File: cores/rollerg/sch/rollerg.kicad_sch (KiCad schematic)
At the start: 1 part

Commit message: wip rollerg sch: objects page
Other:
- added sheet Capacitors (Capacitors.kicad_sch)
- added sheet Not_Populated (Not_Populated.kicad_sch)
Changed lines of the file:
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@@
+	)
+	(sheet
+		(at 246.38 185.42)
+		(size 53.34 20.32)
+		(fields_autoplaced yes)
+		(stroke
+			(width 0.1524)
+			(type solid)
+		)
+		(fill
+			(color 0 0 0 0.0000)
+		)
+		(property "Sheetname" "Capacitors"
+			(at 246.38 184.7084 0)
+			(effects
+				(font
+					(size 3.81 3.81)
+				)
+				(justify left bottom)
+			)
+		)
+		(property "Sheetfile" "Capacitors.kicad_sch"
+			(at 246.38 206.3246 0)
+			(effects
+				(font
+					(size 1.27 1.27)
+				)
+				(justify left top)
+			)
+		)
+		(instances
+			(project "rollerg"
+				(path "/bb61a05c-9ea0-4d47-a326-1f7e835840f3"
+					(page "7")
+				)
+			)
+		)
 	)
 	(sheet
@@
 				)
 			)
+		)
+	)
+	(sheet
+		(at 246.38 215.9)
+		(size 53.34 20.32)
+		(fields_autoplaced yes)
+		(stroke
+			(width 0.1524)
+			(type solid)
+		)
+		(fill
+			(color 0 0 0 0.0000)
+		)
+		(property "Sheetname" "Not_Populated"
+			(at 246.38 215.1884 0)
+			(effects
+				(font
+					(size 3.81 3.81)
+				)
+				(justify left bottom)
+			)
+		)
+		(property "Sheetfile" "Not_Populated.kicad_sch"
+			(at 246.38 236.8046 0)
+			(effects
+				(font
+					(size 1.27 1.27)
+				)
+				(justify left top)
+			)
+		)
+		(instances
+			(project "rollerg"
+				(path "/bb61a05c-9ea0-4d47-a326-1f7e835840f3"
+					(page "8")
+				)
+			)

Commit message: wip rollerg sch: PSAC
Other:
- added sheet IO_Cabinet (IO_Cabinet.kicad_sch)
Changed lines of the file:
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@@
 	)
 	(sheet
-		(at 176.53 33.02)
+		(at 246.38 231.14)
+		(size 53.34 15.24)
+		(fields_autoplaced yes)
+		(stroke
+			(width 0.1524)
+			(type solid)
+		)
+		(fill
+			(color 0 0 0 0.0000)
+		)
+		(property "Sheetname" "IO_Cabinet"
+			(at 246.38 229.1584 0)
+			(effects
+				(font
+					(size 3.81 3.81)
+				)
+				(justify left bottom)
+			)
+		)
+		(property "Sheetfile" "IO_Cabinet.kicad_sch"
+			(at 246.38 246.9646 0)
+			(effects
+				(font
+					(size 1.27 1.27)
+				)
+				(justify left top)
+			)
+		)
+		(instances
+			(project "rollerg"
+				(path "/bb61a05c-9ea0-4d47-a326-1f7e835840f3"
+					(page "9")
+				)
+			)
+		)
+	)
+	(sheet
+		(at 176.53 25.4)
 		(size 52.07 64.77)
 		(fields_autoplaced yes)
@@
 		)
 		(property "Sheetname" "Main"
-			(at 176.53 32.3084 0)
+			(at 176.53 24.6884 0)
 			(effects
 				(font
@@
 		)
 		(property "Sheetfile" "Main.kicad_sch"
-			(at 176.53 98.3746 0)
+			(at 176.53 90.7546 0)
 			(effects
 				(font
@@
 	)
 	(sheet
-		(at 176.53 107.95)
+		(at 176.53 100.33)
 		(size 52.07 68.58)
 		(fields_autoplaced yes)
@@
 		)
 		(property "Sheetname" "Objects"
-			(at 176.53 107.2384 0)
+			(at 176.53 99.6184 0)
 			(effects
 				(font
@@
 		)
 		(property "Sheetfile" "Objects.kicad_sch"
-			(at 176.53 177.1146 0)
+			(at 176.53 169.4946 0)
 			(effects
 				(font
@@
 	)
 	(sheet
-		(at 246.38 107.95)
+		(at 246.38 100.33)
 		(size 53.34 68.58)
 		(fields_autoplaced yes)
@@
 		)
 		(property "Sheetname" "PSAC"
-			(at 246.38 105.9684 0)
+			(at 246.38 98.3484 0)
 			(effects
 				(font
@@
 		)
 		(property "Sheetfile" "PSAC.kicad_sch"
-			(at 246.38 177.1146 0)
+			(at 246.38 169.4946 0)
 			(effects
 				(font
@@
 	)
 	(sheet
-		(at 246.38 33.02)
+		(at 246.38 25.4)
 		(size 53.34 64.77)
 		(fields_autoplaced yes)
@@
 		)
 		(property "Sheetname" "Sound"
-			(at 246.38 31.0384 0)
+			(at 246.38 23.4184 0)
 			(effects
 				(font
@@
 		)
 		(property "Sheetfile" "Sound.kicad_sch"
-			(at 246.38 98.3746 0)
+			(at 246.38 90.7546 0)
 			(effects
 				(font
@@
 	)
 	(sheet
-		(at 246.38 185.42)
-		(size 53.34 20.32)
+		(at 246.38 177.8)
+		(size 53.34 15.24)
 		(fields_autoplaced yes)
 		(stroke
@@
 		)
 		(property "Sheetname" "Capacitors"
-			(at 246.38 184.7084 0)
+			(at 246.38 175.8184 0)
 			(effects
 				(font
@@
 		)
 		(property "Sheetfile" "Capacitors.kicad_sch"
-			(at 246.38 206.3246 0)
+			(at 246.38 193.6246 0)
 			(effects
 				(font
@@
 	)
 	(sheet
-		(at 175.26 185.42)
-		(size 53.34 69.85)
+		(at 176.53 177.8)
+		(size 52.07 69.85)
 		(fields_autoplaced yes)
 		(stroke
@@
 		)
 		(property "Sheetname" "Scroll"
-			(at 175.26 184.7084 0)
+			(at 176.53 175.8184 0)
 			(effects
 				(font
@@
 		)
 		(property "Sheetfile" "Scroll.kicad_sch"
-			(at 175.26 255.8546 0)
+			(at 176.53 248.2346 0)
 			(effects
 				(font
@@
 	)
 	(sheet
-		(at 246.38 215.9)
-		(size 53.34 20.32)
+		(at 246.38 204.47)
+		(size 53.34 15.24)
 		(fields_autoplaced yes)
 		(stroke
@@
 		)
 		(property "Sheetname" "Not_Populated"
-			(at 246.38 215.1884 0)
+			(at 246.38 202.4884 0)
 			(effects
 				(font
@@
 		)
 		(property "Sheetfile" "Not_Populated.kicad_sch"
-			(at 246.38 236.8046 0)
-			(effects
-				(font
+			(at 246.38 220.2946 0)
+			(effects
+				(font

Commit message: wip rollerg sch: SOUND
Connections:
- net COIN_CNT_1: now reaches JM1.8 (COIN_CNT_1)
- net COIN_CNT_2: now reaches JM1.J (COIN_CNT_2)
- no-connect marks 8 -> 6
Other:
- removed sheet Scroll
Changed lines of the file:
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@@
-	)
-	(no_connect
-		(at 54.61 114.3)
 	)
 	(no_connect
@@
 	)
 	(no_connect
-		(at 90.17 114.3)
-	)
-	(no_connect
 		(at 54.61 154.94)
 	)
@@
 	(wire
 		(pts
+			(xy 90.17 114.3) (xy 101.6 114.3)
+		)
+		(stroke
+			(width 0)
+			(type default)
+		)
+	)
+	(wire
+		(pts
 			(xy 100.33 102.87) (xy 100.33 105.41)
 		)
@@
 		(pts
 			(xy 90.17 105.41) (xy 100.33 105.41)
+		)
+		(stroke
+			(width 0)
+			(type default)
+		)
+	)
+	(wire
+		(pts
+			(xy 41.91 114.3) (xy 54.61 114.3)
 		)
 		(stroke
@@
 		)
 	)
+	(label "COIN_CNT_2"
+		(at 101.6 114.3 180)
+		(effects
+			(font
+				(size 1.27 1.27)
+			)
+			(justify right bottom)
+		)
+	)
 	(label "+12V"
 		(at 44.45 110.49 0)
@@
 			)
 			(justify right bottom)
+		)
+	)
+	(label "COIN_CNT_1"
+		(at 41.91 114.3 0)
+		(effects
+			(font
+				(size 1.27 1.27)
+			)
+			(justify left bottom)
 		)
 	)
@@
 	)
 	(sheet
-		(at 246.38 231.14)
-		(size 53.34 15.24)
+		(at 165.1 191.77)
+		(size 52.07 41.91)
 		(fields_autoplaced yes)
 		(stroke
@@
 		)
 		(property "Sheetname" "IO_Cabinet"
-			(at 246.38 229.1584 0)
+			(at 165.1 189.7884 0)
 			(effects
 				(font
@@
 		)
 		(property "Sheetfile" "IO_Cabinet.kicad_sch"
-			(at 246.38 246.9646 0)
+			(at 165.1 234.2646 0)
 			(effects
 				(font
@@
 	)
 	(sheet
-		(at 176.53 25.4)
+		(at 165.1 39.37)
 		(size 52.07 64.77)
 		(fields_autoplaced yes)
@@
 		)
 		(property "Sheetname" "Main"
-			(at 176.53 24.6884 0)
+			(at 165.1 38.6584 0)
 			(effects
 				(font
@@
 		)
 		(property "Sheetfile" "Main.kicad_sch"
-			(at 176.53 90.7546 0)
+			(at 165.1 104.7246 0)
 			(effects
 				(font
@@
 	)
 	(sheet
-		(at 176.53 100.33)
+		(at 165.1 114.3)
 		(size 52.07 68.58)
 		(fields_autoplaced yes)
@@
 		)
 		(property "Sheetname" "Objects"
-			(at 176.53 99.6184 0)
+			(at 165.1 113.5884 0)
 			(effects
 				(font
@@
 		)
 		(property "Sheetfile" "Objects.kicad_sch"
-			(at 176.53 169.4946 0)
+			(at 165.1 183.4646 0)
 			(effects
 				(font
@@
 	)
 	(sheet
-		(at 246.38 100.33)
+		(at 234.95 114.3)
 		(size 53.34 68.58)
 		(fields_autoplaced yes)
@@
 		)
 		(property "Sheetname" "PSAC"
-			(at 246.38 98.3484 0)
+			(at 234.95 112.3184 0)
 			(effects
 				(font
@@
 		)
 		(property "Sheetfile" "PSAC.kicad_sch"
-			(at 246.38 169.4946 0)
+			(at 234.95 183.4646 0)
 			(effects
 				(font
@@
 	)
 	(sheet
-		(at 246.38 25.4)
+		(at 234.95 39.37)
 		(size 53.34 64.77)
 		(fields_autoplaced yes)
@@
 		)
 		(property "Sheetname" "Sound"
-			(at 246.38 23.4184 0)
+			(at 234.95 37.3884 0)
 			(effects
 				(font
@@
 		)
 		(property "Sheetfile" "Sound.kicad_sch"
-			(at 246.38 90.7546 0)
+			(at 234.95 104.7246 0)
 			(effects
 				(font
@@
 	)
 	(sheet
-		(at 246.38 177.8)
+		(at 234.95 191.77)
 		(size 53.34 15.24)
 		(fields_autoplaced yes)
@@
 		)
 		(property "Sheetname" "Capacitors"
-			(at 246.38 175.8184 0)
+			(at 234.95 189.7884 0)
 			(effects
 				(font
@@
 		)
 		(property "Sheetfile" "Capacitors.kicad_sch"
-			(at 246.38 193.6246 0)
+			(at 234.95 207.5946 0)
 			(effects
 				(font
@@
 	)
 	(sheet
-		(at 176.53 177.8)
-		(size 52.07 69.85)
+		(at 234.95 218.44)
+		(size 53.34 15.24)
 		(fields_autoplaced yes)
 		(stroke
@@
 			(color 0 0 0 0.0000)
 		)
-		(property "Sheetname" "Scroll"
-			(at 176.53 175.8184 0)
+		(property "Sheetname" "Not_Populated"
+			(at 234.95 216.4584 0)
 			(effects
 				(font
@@
 			)
 		)
-		(property "Sheetfile" "Scroll.kicad_sch"
-			(at 176.53 248.2346 0)
-			(effects
-				(font
-					(size 1.27 1.27)
-				)
-				(justify left top)
-			)
-		)
-		(instances
-			(project "rollerg"
-				(path "/bb61a05c-9ea0-4d47-a326-1f7e835840f3"
-					(page "4")
-				)
-			)
-		)
-	)
-	(sheet
-		(at 246.38 204.47)
-		(size 53.34 15.24)
-		(fields_autoplaced yes)
-		(stroke
-			(width 0.1524)
-			(type solid)
-		)
-		(fill
-			(color 0 0 0 0.0000)
-		)
-		(property "Sheetname" "Not_Populated"
-			(at 246.38 202.4884 0)
-			(effects
-				(font
-					(size 3.81 3.81)
-				)
-				(justify left bottom)
-			)
-		)
 		(property "Sheetfile" "Not_Populated.kicad_sch"
-			(at 246.38 220.2946 0)
-			(effects
-				(font
+			(at 234.95 234.2646 0)
+			(effects
+				(font

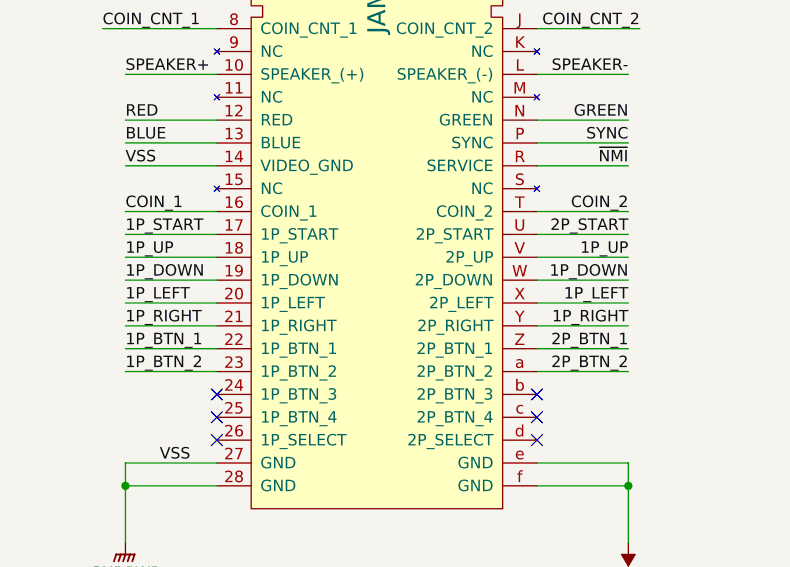
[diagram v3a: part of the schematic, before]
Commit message: wip rollerg sch: CABINET AND RGB
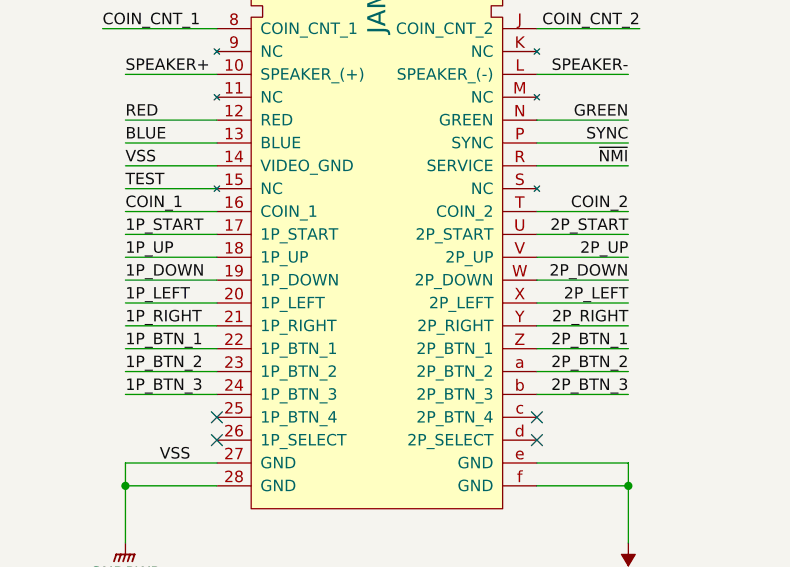
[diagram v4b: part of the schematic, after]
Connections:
- net 1P_DOWN: no longer JM1.W (2P_DOWN)
- net 1P_LEFT: no longer JM1.X (2P_LEFT)
- net 1P_RIGHT: no longer JM1.Y (2P_RIGHT)
- net 1P_UP: no longer JM1.V (2P_UP)
- net TEST: now reaches JM1.15 (NC)
- net 1P_BTN_3: now reaches JM1.24 (1P_BTN_3)
- net 2P_BTN_3: now reaches JM1.b (2P_BTN_3)
- new net 2P_DOWN: JM1.W (2P_DOWN)
- new net 2P_LEFT: JM1.X (2P_LEFT)
- new net 2P_RIGHT: JM1.Y (2P_RIGHT)
- new net 2P_UP: JM1.V (2P_UP)
- no-connect marks 6 -> 4
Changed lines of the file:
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@@
-	)
-	(no_connect
-		(at 90.17 154.94)
 	)
 	(no_connect
@@
 		(at 90.17 157.48)
 	)
-	(no_connect
-		(at 54.61 154.94)
-	)
 	(wire
 		(pts
@@
 	(wire
 		(pts
+			(xy 90.17 154.94) (xy 100.33 154.94)
+		)
+		(stroke
+			(width 0)
+			(type default)
+		)
+	)
+	(wire
+		(pts
 			(xy 44.45 134.62) (xy 54.61 134.62)
 		)
@@
 	(wire
 		(pts
+			(xy 44.45 132.08) (xy 54.61 132.08)
+		)
+		(stroke
+			(width 0)
+			(type default)
+		)
+	)
+	(wire
+		(pts
 			(xy 44.45 110.49) (xy 54.61 110.49)
 		)
@@
 		(pts
 			(xy 100.33 102.87) (xy 100.33 105.41)
+		)
+		(stroke
+			(width 0)
+			(type default)
+		)
+	)
+	(wire
+		(pts
+			(xy 44.45 154.94) (xy 54.61 154.94)
 		)
 		(stroke
@@
 		)
 	)
-	(label "1P_UP"
+	(label "2P_UP"
 		(at 100.33 139.7 180)
 		(effects
@@
 		)
 	)
-	(label "1P_LEFT"
+	(label "2P_LEFT"
 		(at 100.33 144.78 180)
 		(effects
@@
 		)
 	)
+	(label "TEST"
+		(at 44.45 132.08 0)
+		(effects
+			(font
+				(size 1.27 1.27)
+			)
+			(justify left bottom)
+		)
+	)
 	(label "VSS"
 		(at 48.26 97.79 0)
@@
 		)
 	)
-	(label "1P_DOWN"
+	(label "2P_DOWN"
 		(at 100.33 142.24 180)
 		(effects
@@
 		)
 	)
-	(label "1P_RIGHT"
+	(label "2P_RIGHT"
 		(at 100.33 147.32 180)
 		(effects
@@
 		(effects
 			(font
+				(size 1.27 1.27)
+			)
+			(justify right bottom)
+		)
+	)
+	(label "1P_BTN_3"
+		(at 44.45 154.94 0)
+		(effects
+			(font
+				(size 1.27 1.27)
+			)
+			(justify left bottom)
+		)
+	)
+	(label "2P_BTN_3"
+		(at 100.33 154.94 180)
+		(effects
+			(font

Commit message: almost complete rollerg sch
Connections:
- net TEST: now also JM1.11 (NC)
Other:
- sheet IO_Cabinet ports: added 1P_BTN_1, 1P_BTN_2, 1P_BTN_3, 1P_DOWN, 1P_LEFT, 1P_RIGHT, 1P_START, 1P_UP, 2P_BTN_1, 2P_BTN_2, 2P_BTN_3, 2P_DOWN, 2P_LEFT, 2P_RIGHT, 2P_START, 2P_UP, COIN_1, COIN_2, CPU~{EN}, DB[7..0], MAIN_A0, MAIN_A1, MOE, OBCE, OBJSE, TEST, WR, ZOE, ~{DS}, ~{NMI}; removed none
- sheet Main ports: added +12V, +5V, CLK1, CLK2, CLK4, COIN_CNT_1, COIN_CNT_2, DB[7..0], DTAC, G18P15, G18P7, MAIN_A0, MAIN_A1, MAIN_AB[3..0], MAIN_A[23..0], MAIN_D[7..0], MOE, OBJOE, OBJSE, OOE, PAL14, PAL17, RES, R/~{W}, SND_INT, SYNC, ZOE, ~{AS}, ~{CLK2}, ~{CS1}, ~{DS}, ~{HBK}, ~{HSYNC}, ~{MCS}, ~{OBJSET}, ~{OBJ_CS}, ~{VBK}, ~{VSYNC}; removed none
- sheet Objects ports: added CLK2, CPU~{EN}, DB[7..0], M12B, MAIN_AB[3..0], MAIN_A[12..0], MAIN_D[7..0], OBJPXL[7..0], OBOB, OBOK, OOE, RES, R/~{W}, SDI0, VD6, ~{CS1}, ~{DS}, ~{HSYNC}, ~{OBJSET}, ~{OBJ_CS}, ~{RD}, ~{VSYNC}; removed none
- sheet PSAC ports: added BLUE, CLK1, CLK2, CLK4, DB[7..0], DTAC, G18P15, G18P7, GREEN, M12B, MAIN_A[10..0], OBCE, OBJOE, OBJPXL[7..0], OBJSE, OBOB, OBOK, PAL14, PAL17, RED, RES, R/~{W}, SDI0, VD6, WR, ~{AS}, ~{CLK2}, ~{DS}, ~{HBK}, ~{HSYNC}, ~{RD}, ~{VBK}, ~{VSYNC}; removed none
- sheet Sound ports: added +12V, DB[7..0], MAIN_A1, RES, R/~{W}, SND_INT, SPEAKER+, SPEAKER-, ~{MCS}, ~{RD}; removed none
